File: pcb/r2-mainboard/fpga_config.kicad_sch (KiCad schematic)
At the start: 32 parts, among them U41 XC6SLX-FTG256, U42 W25Q128JVSIQ, X1 33.33MHz

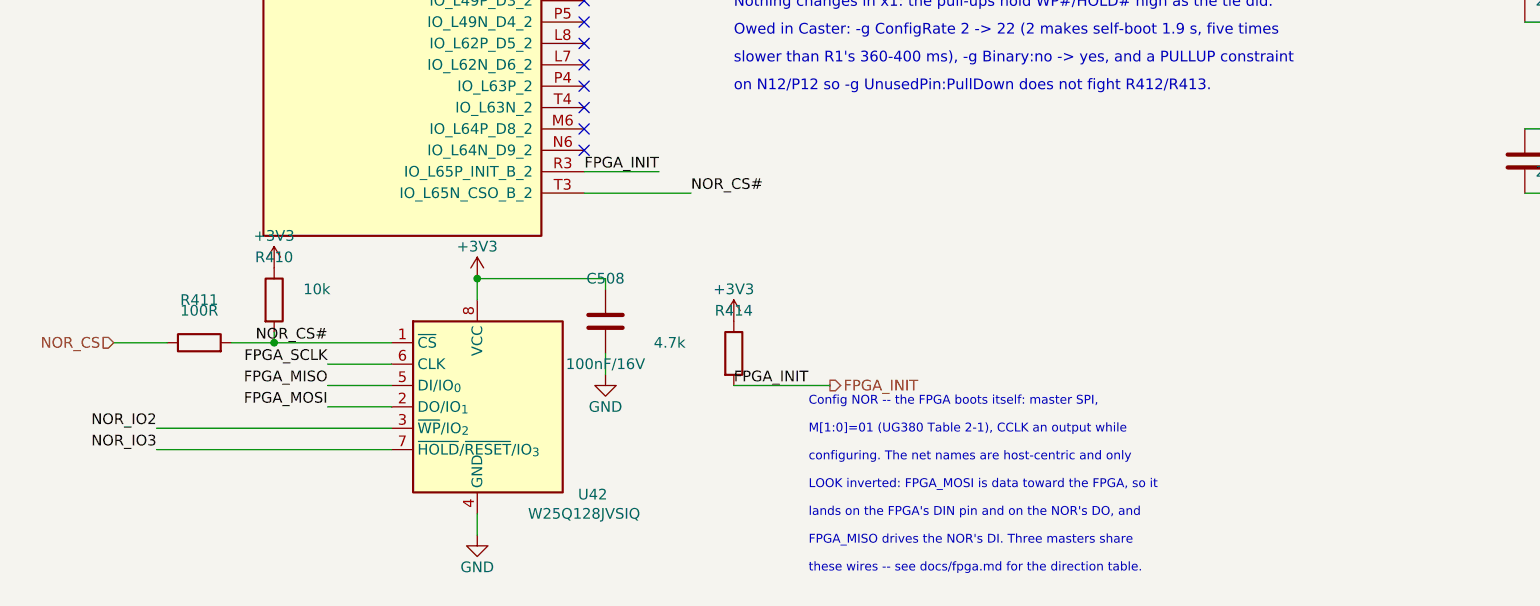
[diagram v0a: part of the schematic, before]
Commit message: Docs: library audit list and a first production costing
libraries.md -- every symbol in r2.kicad_sym and every footprint in
r2.pretty, with what it was derived from, which tools/ script emits it,
and what was actually checked. Written for the owner's audit before the
libraries get rehomed. Notes that pcb_common has never been modified,
and calls out the three newest entries (TPS2553DBV and the two
_Mirrored FPC land patterns) as the least reviewed.

NOTES-production-costing.md -- what 1000 units costs and what a campaign
would have to raise, prompted by Good Display's US$750 / MOQ 1000 quote.
Central estimate EUR 340/unit COGS and a EUR ~548k goal, but the honest
finding is the sensitivity: the PCM-071 at EUR 250 @1-9 costs more than
the display, and the sibling quote says ~EUR 190 of that is a memory-
shortage surcharge. A 1000-piece quote moves the goal by EUR 290k, so it
is the single highest-value thing to chase. Also states plainly that at
the central estimate the margin is thin to negative against market
comparables, and what to do about it.

Both indexed in CLAUDE.md.

Co-Authored-By: Claude Opus 5 <noreply@anthropic.com>
Claude-Session: https://claude.ai/code/session_01MHTAe6ZnhogTEgtyPcLhwG
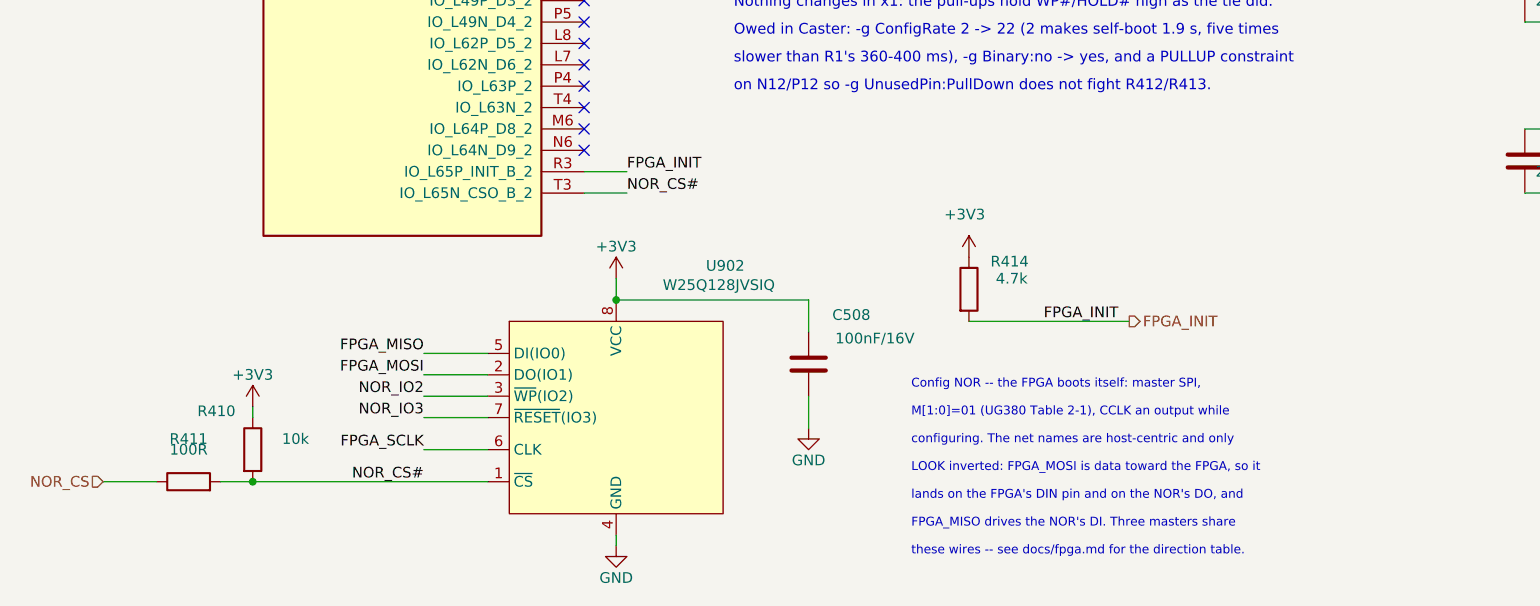
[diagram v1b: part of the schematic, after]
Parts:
- U902: renamed from U42; footprint Package_SO:SOIC-8_5.3x5.3mm_P1.27mm -> Reflow:QSPI Flash SOIC; symbol Memory_Flash:W25Q128JVS -> Reflow:WSON_Flash
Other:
- moved on the sheet: C508, R410, R411, R414, U902

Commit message: R2: renumber every sheet to the page-based designator scheme
The owner's scheme is classifier + sheet page + two-digit part from 00. Four
sheets already used it; this converts the remaining nine, so all thirteen now
agree: pages 2-9 take three digits, pages 10-14 four. 292 of 333 designators
changed. A part shared by several sheets takes its lowest page, so the FPGA is
U700 (pages 7-9) and the two SoM connectors are J501/J502 (pages 5-6).

The whole risk here is silently rewiring the board, so the netlist was diffed
rather than eyeballed:

  nets 519 -> 519, total pin connections 1563 -> 1563
  named nets present in both whose pin multiset changed: 0
  ERC unchanged at 14 errors / 20 warnings
  check_ucf.py: 99 balls matched, 0 failures

That last one matters most: it resolves the gateware's 113 UCF constraints to
board nets *by ball name*, so it is the sharpest detector of the corruption
this change could cause.

Two earlier attempts did cause exactly that. A bare quoted-string substitution
also rewrites FPGA ball names (C1, D2, N11, T1) and BTH-060 pin names (A1-D60),
which are spelled exactly like designators; one run left ERC identical while 40
nets came back with a different pin multiset. The tool now substitutes only at
the two positions that store an instance's designator, and excludes every pin
name everywhere else. docs/layout.md 9.5 records the hazard and how to prove a
renumber was clean.

Only the three scripts that read the design are updated. The gen_*/patch_*/
port_r1.py scripts keep the old names deliberately: each wrote a sheet once and
has not been re-runnable since it was hand-edited in Eeschema, so they are a
historical record -- and port_r1.py's dict keys are R1 designators that were
never renumbered at all.

Co-Authored-By: Claude Opus 5 <noreply@anthropic.com>
Claude-Session: https://claude.ai/code/session_01MHTAe6ZnhogTEgtyPcLhwG
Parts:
- renumbered C316 to C900, C326 to C901, C392 to C902, C393 to C903, C448 to C904, C449 to C905, C450 to C906, C456 to C907, C457 to C908, C482 to C909, C483 to C910, C484 to C911, C485 to C912, C486 to C913, C487 to C914, C488 to C915, C489 to C916, C490 to C917, C507 to C918, C508 to C919, R335 to R900, R336 to R901, R337 to R902, R409 to R903, R410 to R904, R411 to R905, R412 to R906, R413 to R907, R414 to R908, U41 to U700, X1 to X900
